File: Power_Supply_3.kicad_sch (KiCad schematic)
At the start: 8 parts

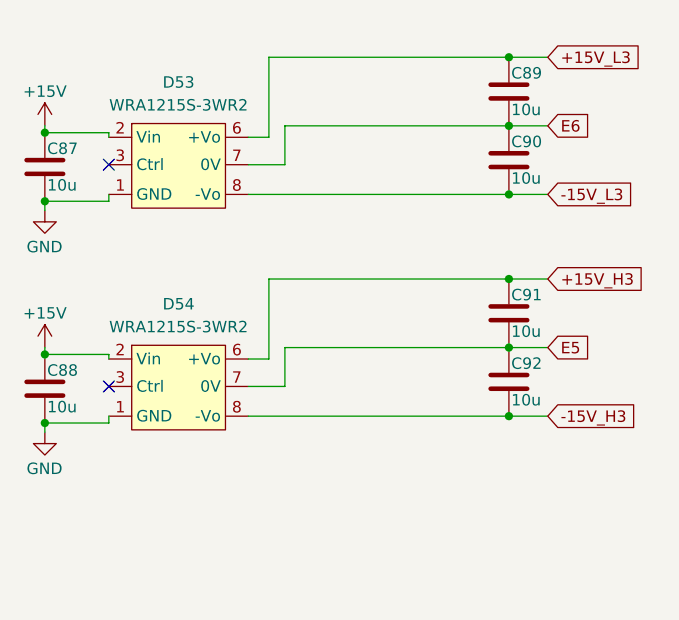
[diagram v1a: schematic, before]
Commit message: Изменил схему
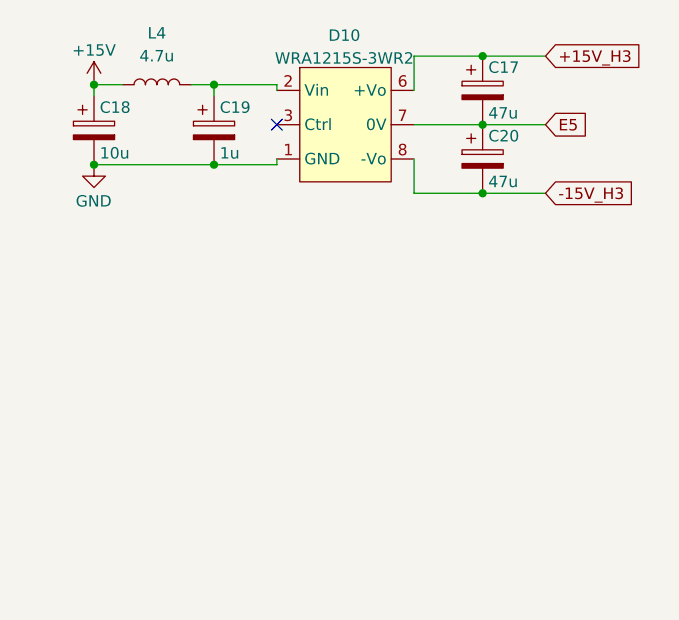
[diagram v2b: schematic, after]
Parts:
- removed C87, C88, C89, C90, C91, C92: 10u, Capacitor_SMD:C_1210_3225Metric_Pad1.33x2.70mm_HandSolder, symbol Device:C
- removed D53, D54: WRA1215S-3WR2, Mornsun:WRA1215S-3WR2, symbol Morsun:WRA1215S-3WR2
- added C17, C20: 47u, Capacitor_Tantalum_SMD:CP_EIA-7343-31_Kemet-D, symbol Device:C_Polarized
- added C18: 10u, Capacitor_Tantalum_SMD:CP_EIA-7343-31_Kemet-D, symbol Device:C_Polarized
- added C19: 1u, Capacitor_Tantalum_SMD:CP_EIA-3528-21_Kemet-B, symbol Device:C_Polarized
- added D10: WRA1215S-3WR2, Mornsun:WRA_S-3WR2, symbol Morsun:WRA1215S-3WR2
- added L4: 4.7u, Inductor_SMD:L_1812_4532Metric_Pad1.30x3.40mm_HandSolder, symbol Device:L
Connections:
- net +15V: now also C18.1, L4.1
- net +15V_H3: now also C17.1, D10.6 (+Vo)
- net -15V_H3: now also C20.2, D10.8 (-Vo)
- net E5: now also C17.2, C20.1, D10.7 (0V)
- net GND: now also C18.2, C19.2, D10.1 (GND)
- new net: C19.1, D10.2 (Vin), L4.2
- no-connect marks 2 -> 1

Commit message: Разместил все три стойки в своей области
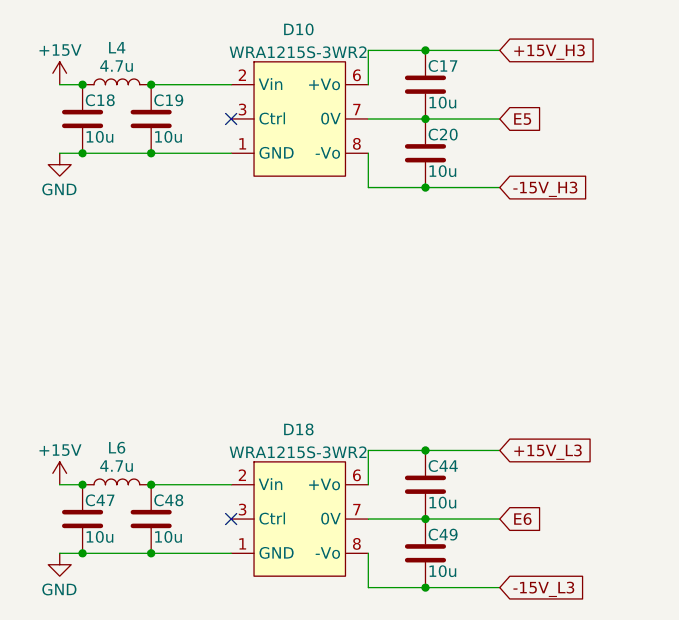
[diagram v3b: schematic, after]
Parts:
- removed C17, C20: 47u, Capacitor_Tantalum_SMD:CP_EIA-7343-31_Kemet-D, symbol Device:C_Polarized
- removed C18: 10u, Capacitor_Tantalum_SMD:CP_EIA-7343-31_Kemet-D, symbol Device:C_Polarized
- removed C19: 1u, Capacitor_Tantalum_SMD:CP_EIA-3528-21_Kemet-B, symbol Device:C_Polarized
- added C17, C18, C19, C20, C44, C47, C48, C49: 10u, Capacitor_SMD:C_1210_3225Metric_Pad1.33x2.70mm_HandSolder, symbol Device:C
- added D18: WRA1215S-3WR2, Mornsun:WRA_S-3WR2, symbol Morsun:WRA1215S-3WR2
- added L6: 4.7u, Inductor_SMD:L_1812_4532Metric_Pad1.30x3.40mm_HandSolder, symbol Device:L
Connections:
- net +15V: now also C18.1, C47.1, L6.1
- net +15V_H3: now also C17.1
- net -15V_H3: now also C20.2
- net E5: now also C17.2, C20.1
- net GND: now also C18.2, C19.2, C47.2, C48.2, D18.1 (GND)
- net at D10.2 (Vin), L4.2: now also C19.1
- new net: C48.1, D18.2 (Vin), L6.2
- new net +15V_L3: C44.1, D18.6 (+Vo)
- new net -15V_L3: C49.2, D18.8 (-Vo)
- new net E6: C44.2, C49.1, D18.7 (0V)
- no-connect marks 1 -> 2

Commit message: VER2.1: добавил схему в доки
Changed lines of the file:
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@@
 (kicad_sch
-	(version 20231120)
+	(version 20250114)
 	(generator "eeschema")
-	(generator_version "8.0")
+	(generator_version "9.0")
 	(paper "A4")
 	(junction
